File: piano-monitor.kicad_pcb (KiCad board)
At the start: 2 copper layers, 169.1 x 74.8 mm, 6 parts, among them J3 NCJ6FA-V, J4 DC, J7 NCJ6FA-V

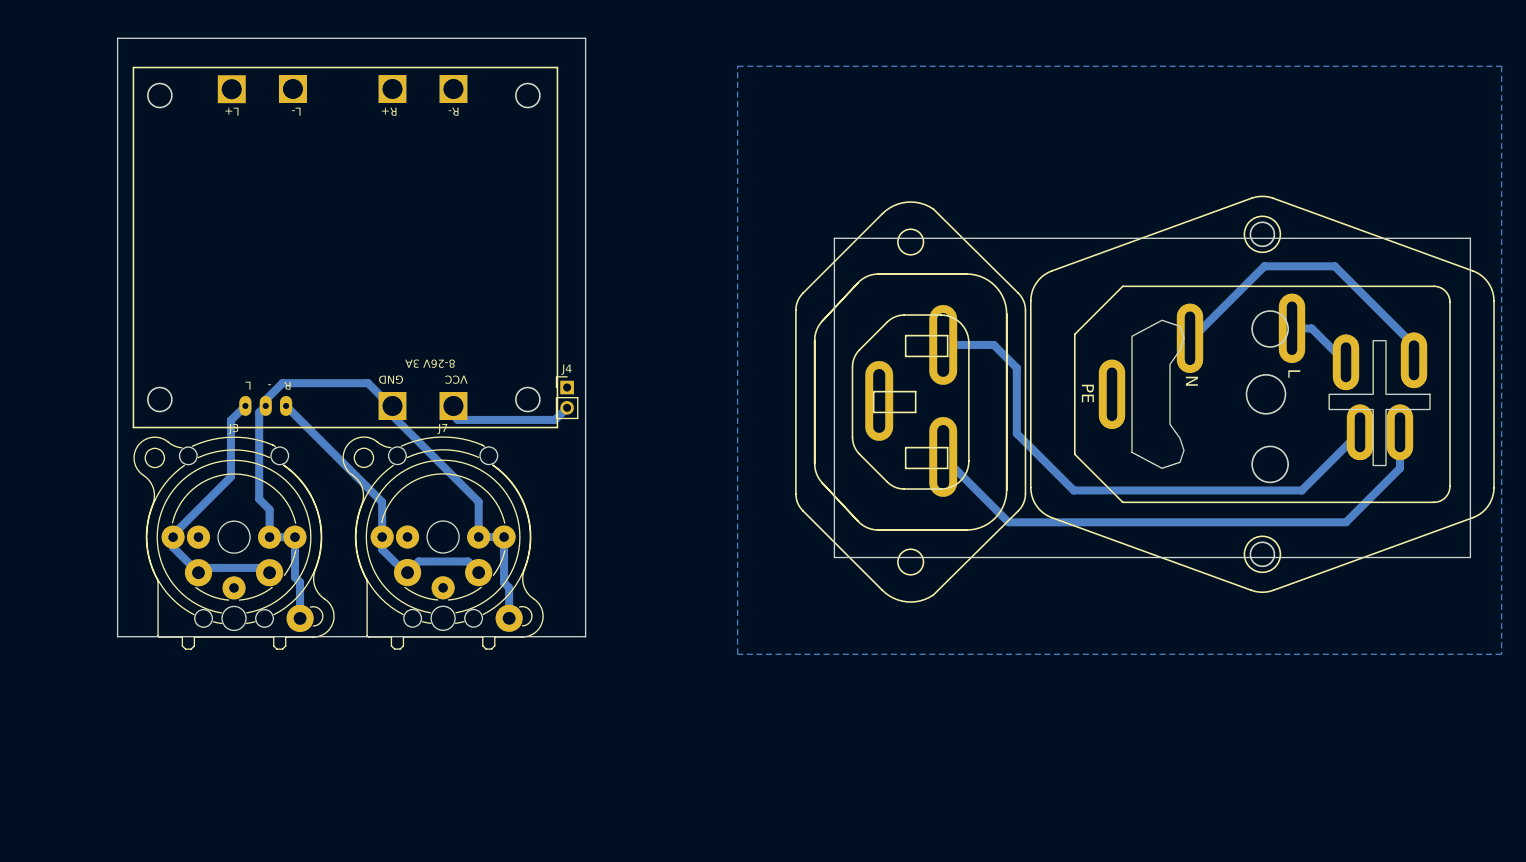
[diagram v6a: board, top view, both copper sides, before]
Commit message: Update schematic and prepare for the AC pcb to be milled out with a 0.8mm bit
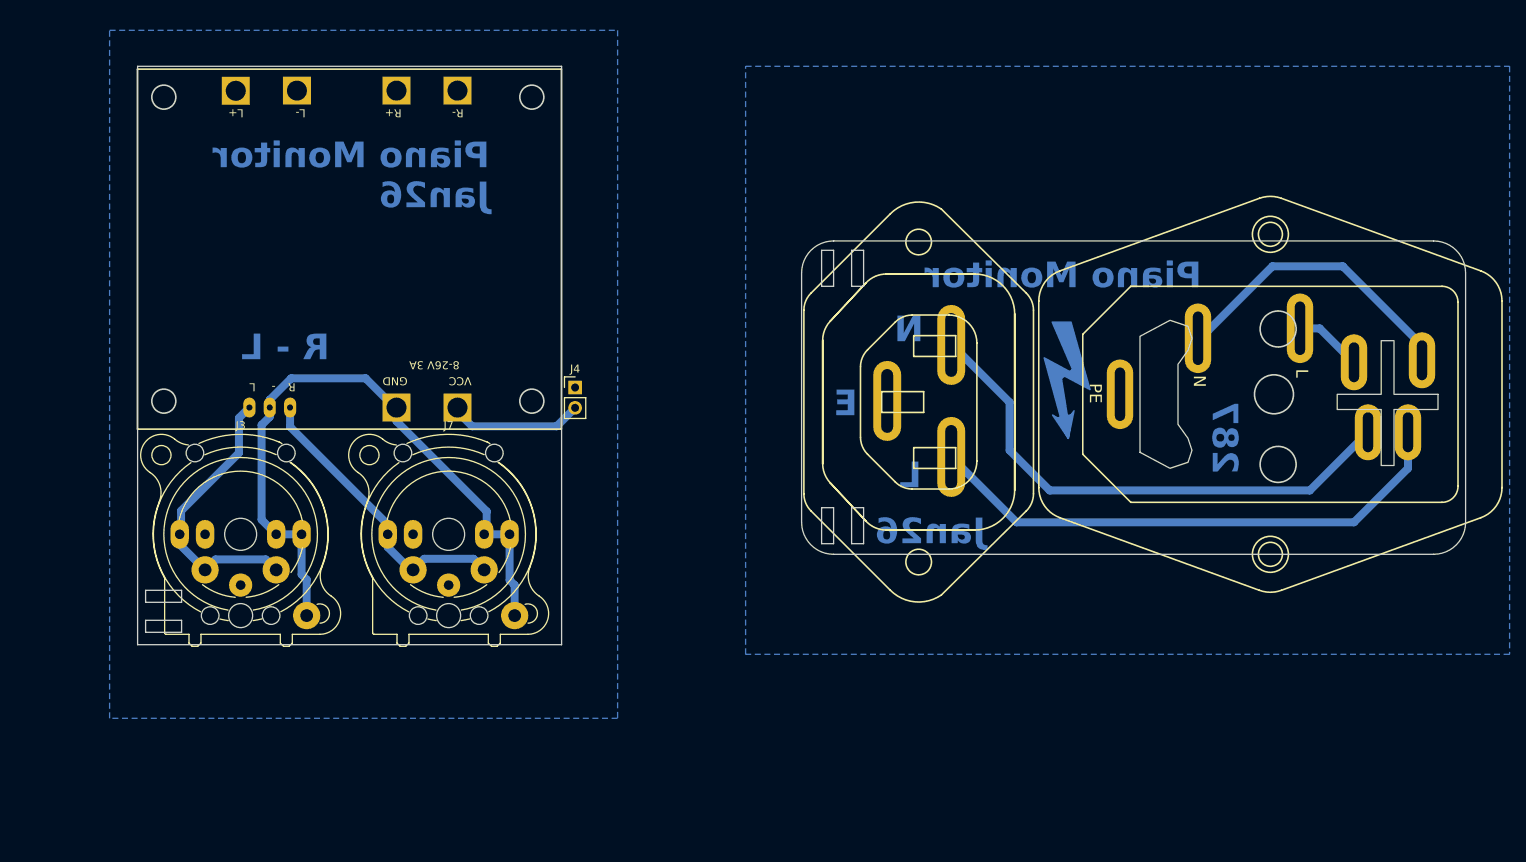
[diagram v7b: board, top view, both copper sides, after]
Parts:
- added REF**: Symbol_HighVoltage_NoTriangle_6x15mm_Copper, Symbol:Symbol_HighVoltage_NoTriangle_6x15mm_Copper, B.Cu at (229.0, 94.0)
- moved J1 1.00 mm to (255.1, 96.0)
- moved J4 1.00 mm to (167.7, 95.2)
- moved J6 1.00 mm to (210.6, 96.9)
- moved J3 0.90 mm to (133.5, 113.5)
- moved J7 0.77 mm to (159.5, 113.5)
- moved U1 0.54 mm to (139.5, 78.0)
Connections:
- net Earth renamed EARTH
- net Net-(J1-A) renamed L_PRESWITCH
- net Net-(J1-B) renamed N_PRESWITCH
- J3 pad 3: R2 -> unconnected-(J3-Pad3)
- J3 pad R: R2 -> unconnected-(J3-PadR)
- J7 pad 3: R1 -> unconnected-(J7-Pad3)
- J7 pad R: R1 -> unconnected-(J7-PadR)
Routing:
- net N: track 67.4 -> 66.2 mm
- net +24V: track 16.3 -> 16.9 mm
- added copper zone on B.Cu, net GND
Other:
- board size 169.1 x 74.8 mm -> 166 x 72.3 mm
- board text added: "287"
- board text added: "E"
- board text added: "Jan26"
- board text added: "L"
- board text added: "N"
- board text added: "Piano Monitor"
- board text added: "R - L"
